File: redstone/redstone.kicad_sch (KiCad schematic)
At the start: 21 parts, among them J1 Conn_01x04_MountingPin, J2 Conn_01x04_MountingPin, J3 Conn_01x04_MountingPin, J4 Conn_01x04_MountingPin, J5 Conn_01x04_MountingPin, J6 Conn_01x04_MountingPin, J7 Conn_01x04_MountingPin, J8 Conn_01x04_MountingPin, Q1 BC108, U1 RP2040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

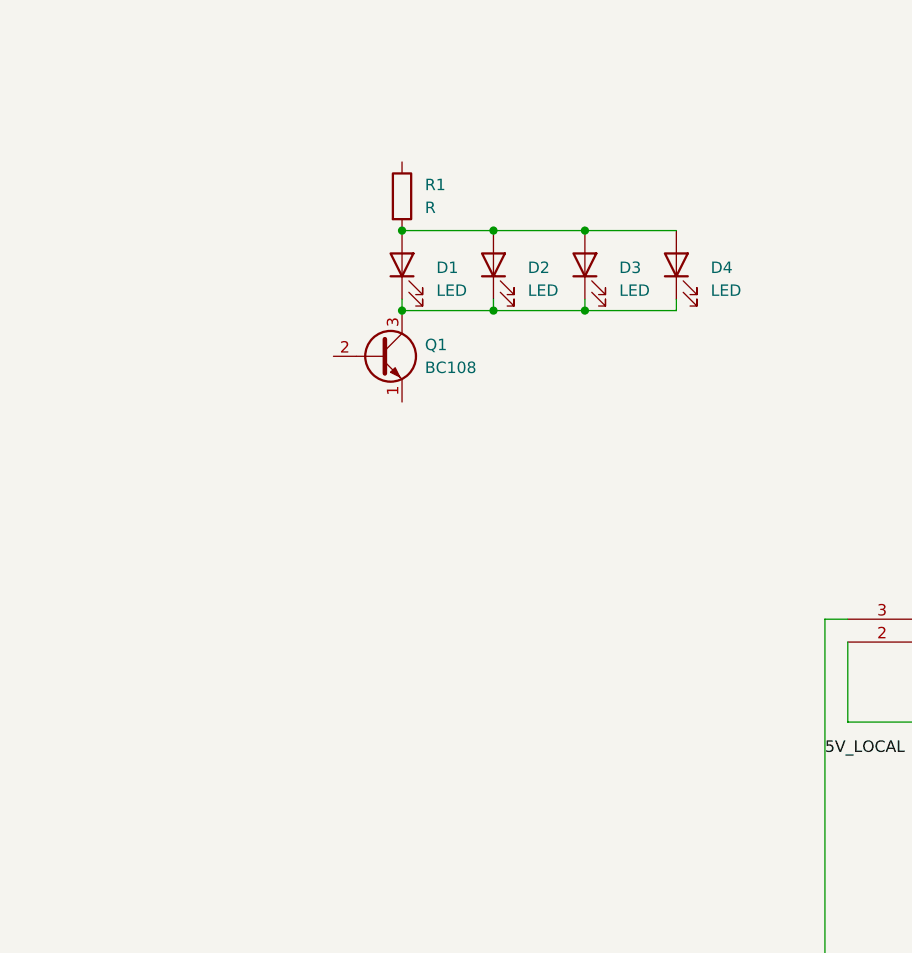
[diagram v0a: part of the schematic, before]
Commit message: add more leds
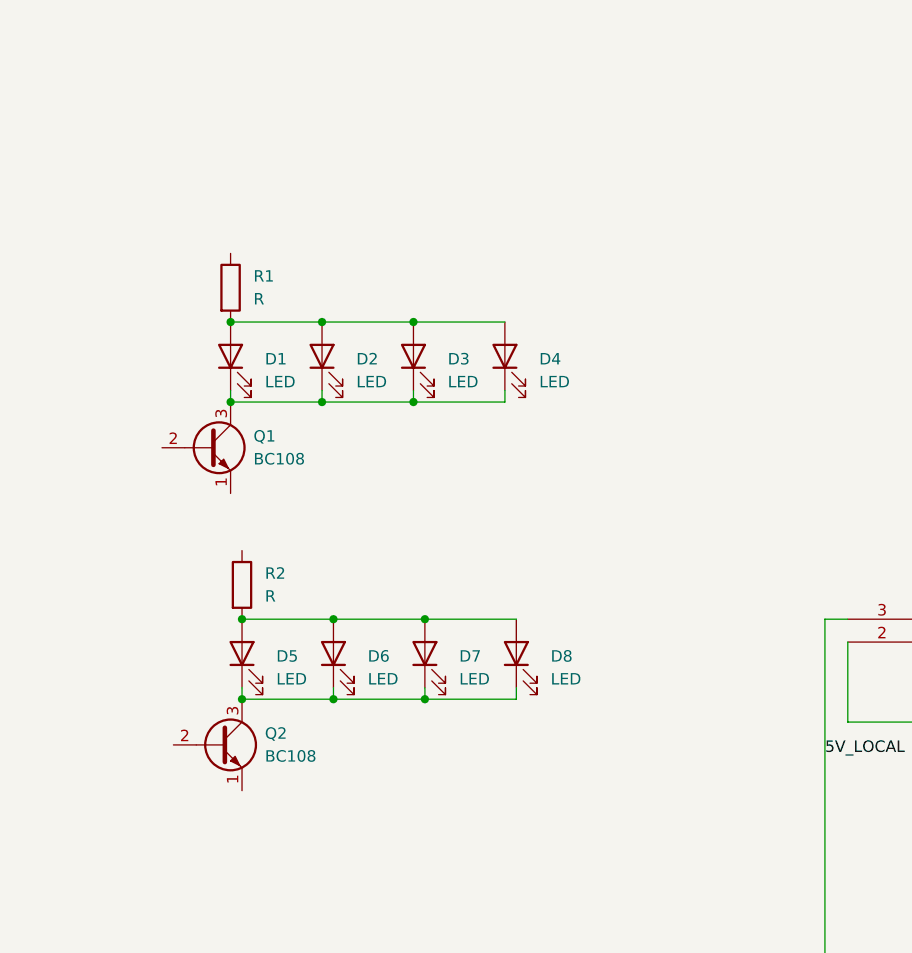
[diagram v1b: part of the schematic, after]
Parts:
- added D5, D6, D7, D8: LED, symbol Device:LED
- added Q2: BC108, Package_TO_SOT_THT:TO-18-3, symbol Transistor_BJT:BC108
- added R2: R, symbol Device:R
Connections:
- new net: D5.1 (K), D6.1 (K), D7.1 (K), D8.1 (K), Q2.3 (C)
- new net: D5.2 (A), D6.2 (A), D7.2 (A), D8.2 (A), R2.2
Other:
- moved on the sheet: D1, D2, D3, D4, Q1, R1

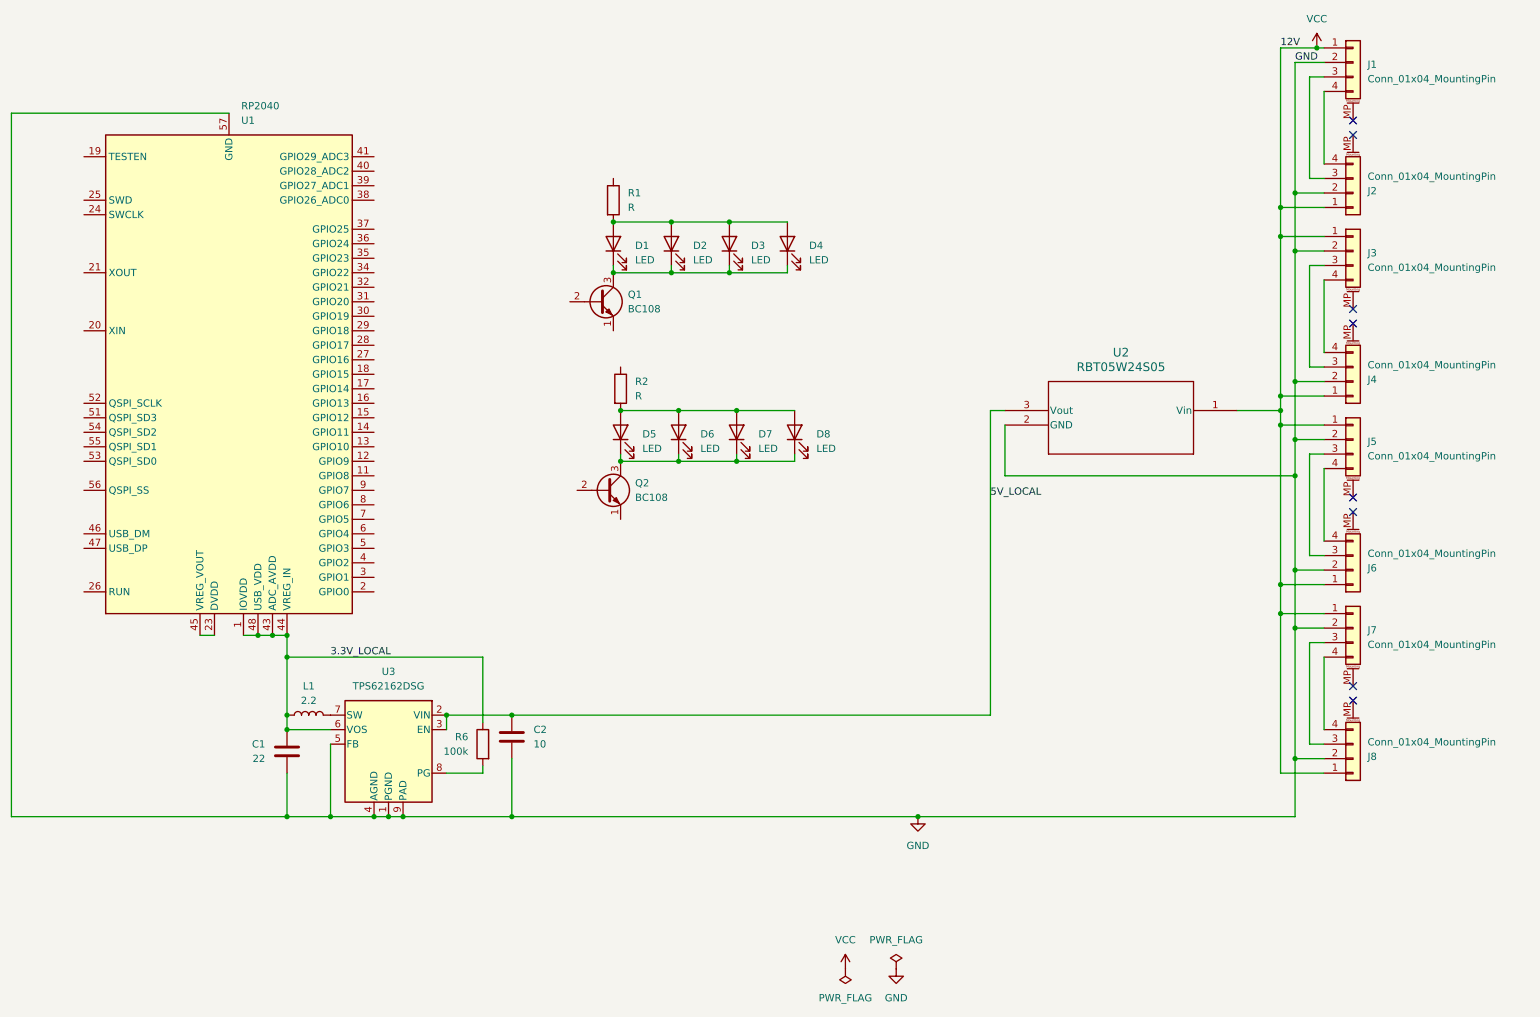
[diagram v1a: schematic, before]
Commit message: add tx rx wiring, add flash memory
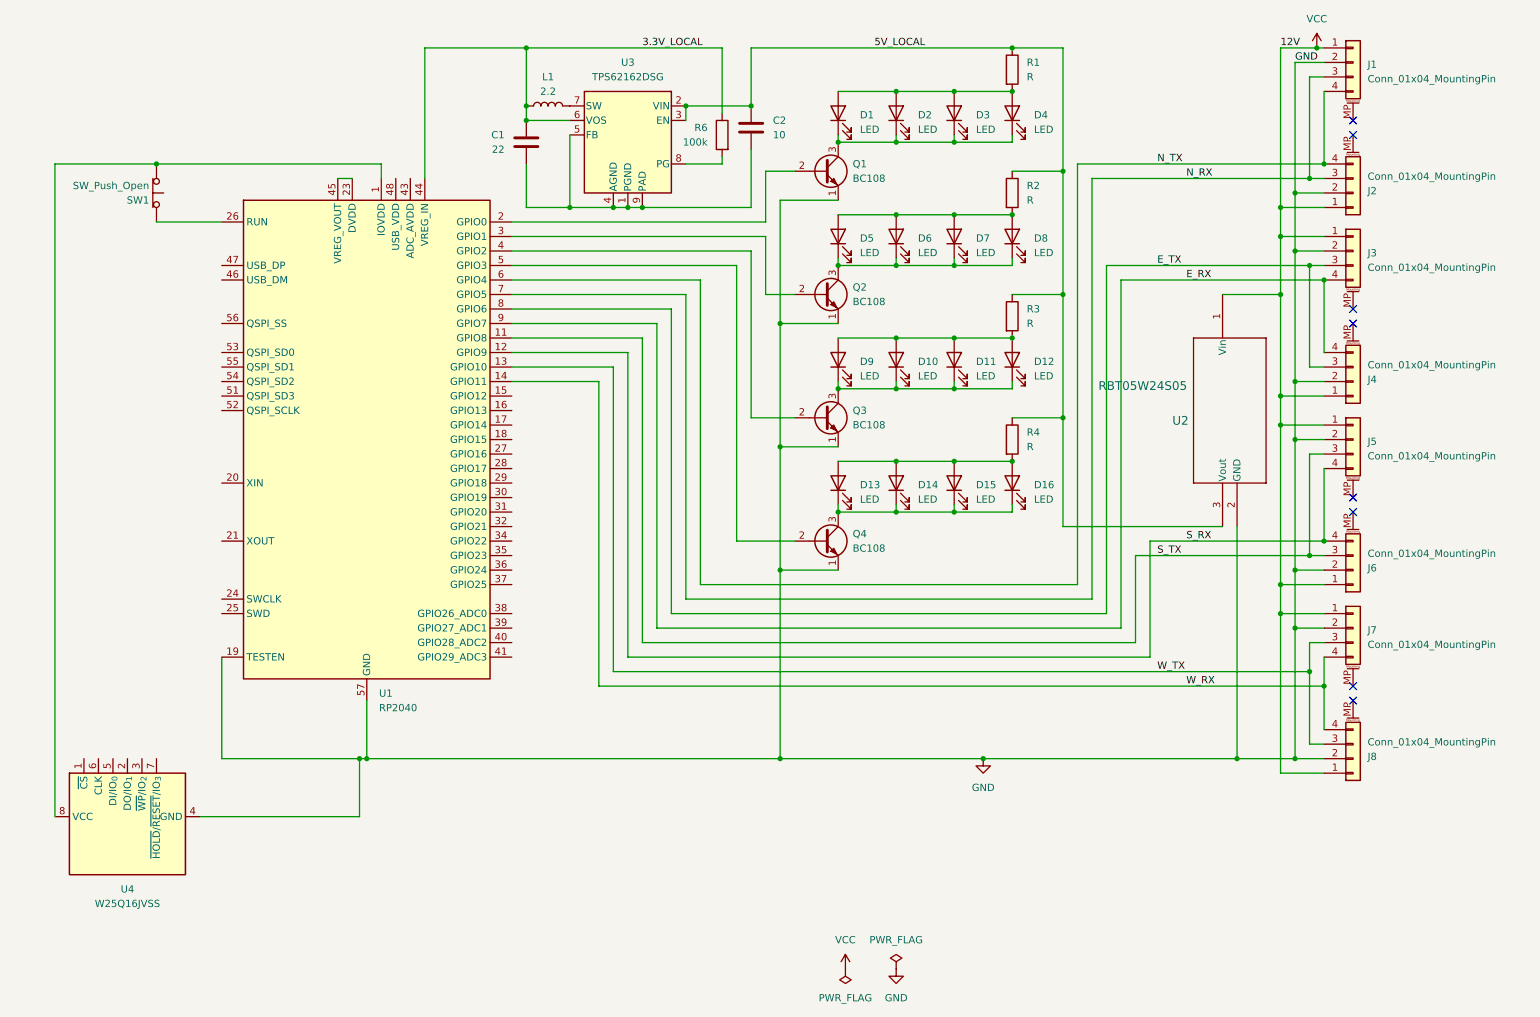
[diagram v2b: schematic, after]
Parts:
- added D10, D11, D12, D13, D14, D15, D16, D9: LED, symbol Device:LED
- added Q3, Q4: BC108, Package_TO_SOT_THT:TO-18-3, symbol Transistor_BJT:BC108
- added R3, R4: R, symbol Device:R
- added SW1: SW_Push_Open, symbol Switch:SW_Push_Open
- added U4: W25Q16JVSS, Package_SO:SOIC-8_5.3x5.3mm_P1.27mm, symbol Memory_Flash:W25Q16JVSS
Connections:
- net 3.3V_LOCAL: no longer U1.1 (IOVDD), U1.10 (IOVDD), U1.22 (IOVDD), U1.33 (IOVDD), U1.42 (IOVDD), U1.43 (ADC_AVDD), U1.48 (USB_VDD), U1.49 (IOVDD)
- net 5V_LOCAL: now also R1.1, R2.1, R3.1, R4.1
- net GND: now also Q1.1 (E), Q2.1 (E), U1.19 (TESTEN), Q3.1 (E), Q4.1 (E), U4.4 (GND); no longer C1.2, C2.1, U3.1 (PGND), U3.4 (AGND), U3.5 (FB), U3.9 (PAD)
- net W_TX: now reaches J7.3 (Pin_3), J8.3 (Pin_3)
- net W_TX: now also U1.13 (GPIO10)
- net W_RX: now reaches J7.4 (Pin_4), J8.4 (Pin_4)
- net W_RX: now also U1.14 (GPIO11)
- net S_TX: now reaches J5.3 (Pin_3), J6.3 (Pin_3)
- net S_TX: now also U1.11 (GPIO8)
- net S_RX: now reaches J5.4 (Pin_4), J6.4 (Pin_4)
- net S_RX: now also U1.12 (GPIO9)
- net E_TX: now reaches J3.3 (Pin_3), J4.3 (Pin_3)
- net E_TX: now also U1.8 (GPIO6)
- net E_RX: now reaches J3.4 (Pin_4), J4.4 (Pin_4)
- net E_RX: now also U1.9 (GPIO7)
- net at Q1.2 (B): now also U1.2 (GPIO0)
- net N_RX: now reaches J1.3 (Pin_3), J2.3 (Pin_3)
- net N_RX: now also U1.7 (GPIO5)
- net N_TX: now reaches J1.4 (Pin_4), J2.4 (Pin_4)
- net N_TX: now also U1.6 (GPIO4)
- net at Q2.2 (B): now also U1.3 (GPIO1)
- net at U1.26 (RUN): now also SW1.2 (B)
- net at U1.4 (GPIO2): now also Q3.2 (B)
- net at U1.5 (GPIO3): now also Q4.2 (B)
- new net: D13.2 (A), D14.2 (A), D15.2 (A), D16.2 (A), R4.2
- new net: C1.2, C2.1, U3.1 (PGND), U3.4 (AGND), U3.5 (FB), U3.9 (PAD)
- new net: D13.1 (K), D14.1 (K), D15.1 (K), D16.1 (K), Q4.3 (C)
- new net: SW1.1 (A), U1.1 (IOVDD), U1.10 (IOVDD), U1.22 (IOVDD), U1.33 (IOVDD), U1.42 (IOVDD), U1.49 (IOVDD), U4.8 (VCC)
- new net: D10.1 (K), D11.1 (K), D12.1 (K), D9.1 (K), Q3.3 (C)
- new net: D10.2 (A), D11.2 (A), D12.2 (A), D9.2 (A), R3.2
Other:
- moved on the sheet: C1, C2, D1, D2, D3, D4, L1, Q1, R1, R6, U1, U2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

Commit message: connect flash memory
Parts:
- added U5: W25Q16JVSS, Package_SO:SOIC-8_5.3x5.3mm_P1.27mm, symbol Memory_Flash:W25Q16JVSS
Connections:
- net GND: now also U5.4 (GND); no longer U4.4 (GND)
- net at SW1.1 (A), U1.1 (IOVDD), U1.10 (IOVDD)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: now also U5.8 (VCC); no longer U4.8 (VCC)
- net at U1.51 (QSPI_SD3): now also U5.7 (~{HOLD}/~{RESET}/IO_{3})
- net at U1.52 (QSPI_SCLK): now also U5.6 (CLK)
- net at U1.53 (QSPI_SD0): now also U5.5 (DI/IO_{0})
- net at U1.54 (QSPI_SD2): now also U5.3 (~{WP}/IO_{2})
- net at U1.55 (QSPI_SD1): now also U5.2 (DO/IO_{1})
- net at U1.56 (QSPI_SS): now also U5.1 (~{CS})
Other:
- moved on the sheet: SW1, U1
